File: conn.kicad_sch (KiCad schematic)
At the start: 73 parts, among them J10 MicroFit_2x04, J11 JST_S4B-XH, J12 MicroFit_2x04, J13 JST_B2B-XH, J14 JST_S2B-XH, J15 DNI, J16 MLX_1x03, J17 MLX_1x03, J5 JST_S6B-XH, J6 JST_S4B-XH, J7 MicroFit_2x04, J8 JST_S4B-XH, J9 JST_S4B-XH, SW2 DNI

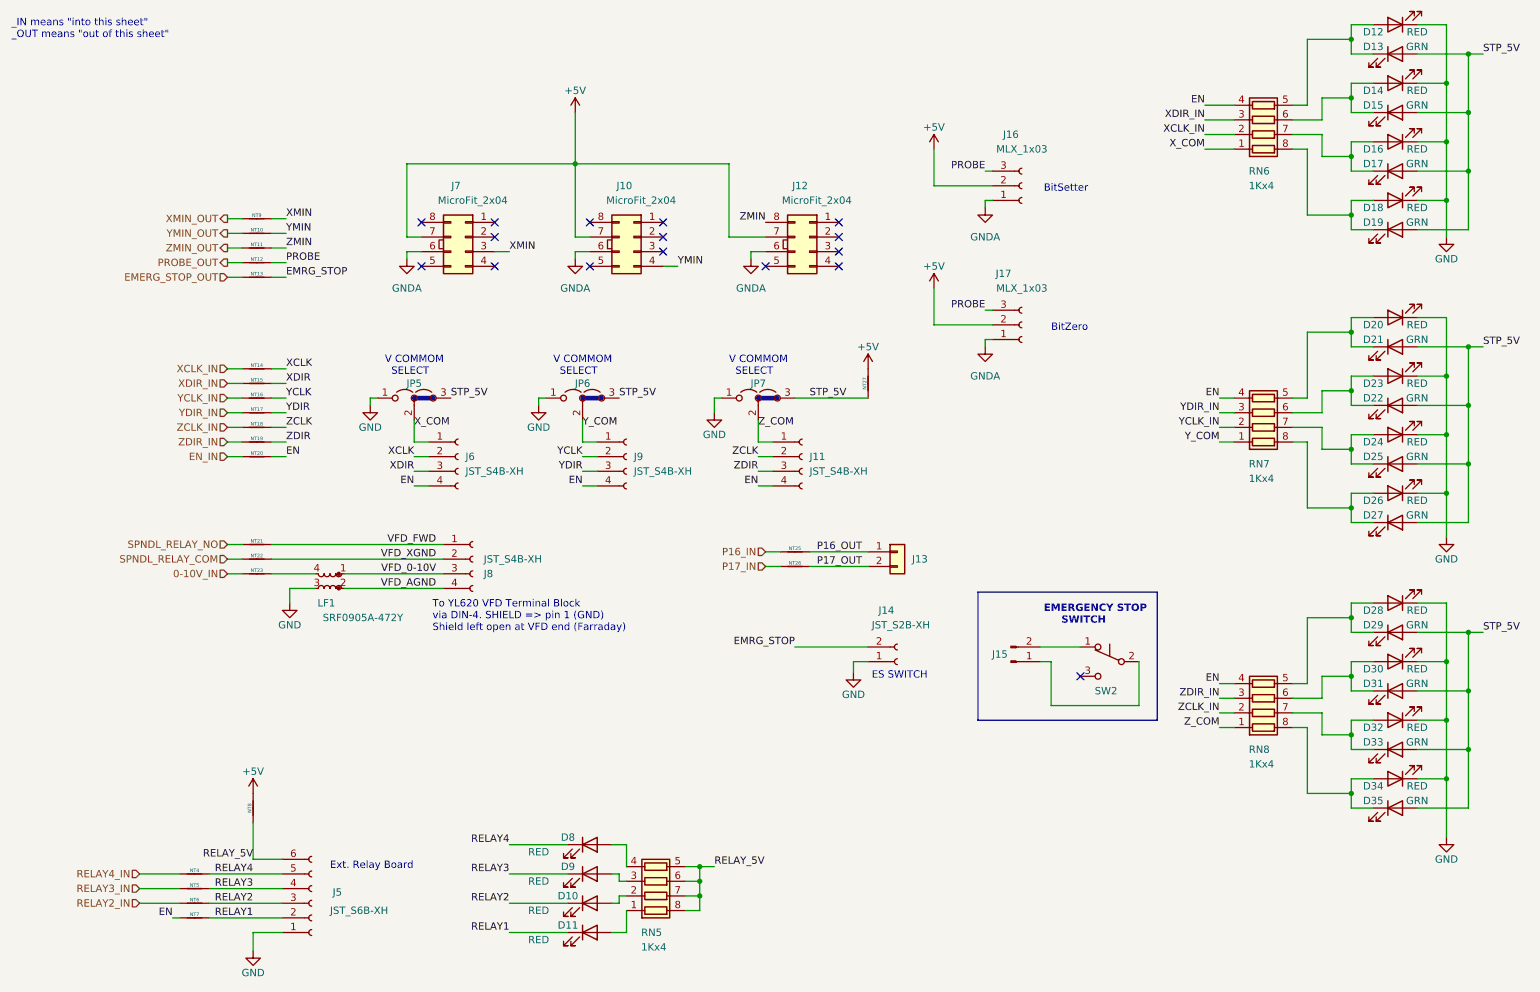
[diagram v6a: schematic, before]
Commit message: Completed change to screw terminal blocks. (P16/17 remains JST.)
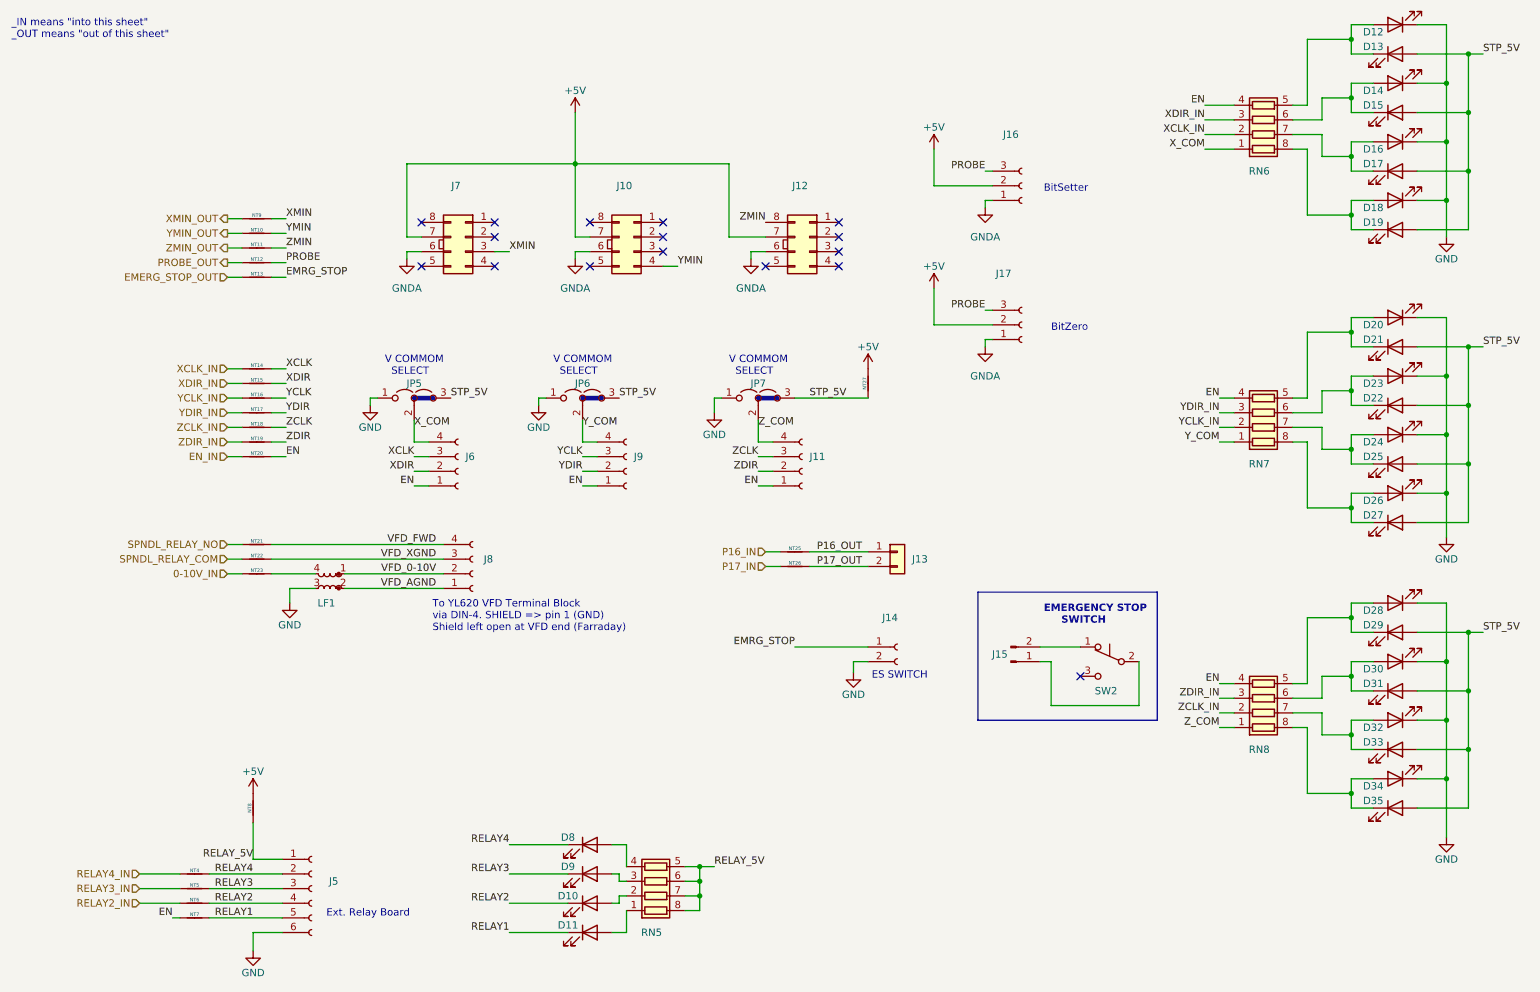
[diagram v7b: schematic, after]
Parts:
- D10, D11, D12, D14, D16, D18, D20, D22, D24, D26, D28, D30, D32, D34, D8, D9: value RED -> (none); footprint -Project:LED_0402_DOT -> (none)
- D13, D15, D17, D19, D21, D23, D25, D27, D29, D31, D33, D35: value GRN -> (none); footprint -Project:LED_0402_DOT -> (none)
- J10, J12, J7: value MicroFit_2x04 -> (none); footprint Connector_Molex:Molex_Micro-Fit_3.0_43045-0812_2x04_P3.00mm_Vertical -> (none)
- J11, J6, J8, J9: value JST_S4B-XH -> (none); footprint Connector_JST:JST_EH_S4B-EH_1x04_P2.50mm_Horizontal -> (none); E14MFR# S4B-EH(LF)(SN) -> (none); E14PART 1830721 -> (none); JLCMFR# S4B-XH-A(LF)(SN) -> (none); JLCPART C157925 -> (none)
- J13: value JST_B2B-XH -> (none); footprint Connector_JST:JST_EH_B2B-EH-A_1x02_P2.50mm_Vertical -> (none)
- J14: value JST_S2B-XH -> (none); footprint Connector_JST:JST_EH_S2B-EH_1x02_P2.50mm_Horizontal -> (none)
- J15, SW2: value DNI -> (none)
- J16, J17: value MLX_1x03 -> (none); footprint Connector_Molex:Molex_KK-254_AE-6410-03A_1x03_P2.54mm_Vertical -> (none)
- J5: value JST_S6B-XH -> (none); footprint Connector_JST:JST_EH_S6B-EH_1x06_P2.50mm_Horizontal -> (none); E14PART 1516282 -> (none); JLCMFR# S6B-XH-A(LF)(SN) -> (none); JLCPART C157919 -> (none)
- JP5, JP6, JP7: value Jumper_3_Open -> (none); footprint Connector_PinHeader_2.54mm:PinHeader_1x03_P2.54mm_Vertical -> (none)
- LF1: value SRF0905A-472Y -> (none); footprint Filter:Filter_Bourns_SRF0905_6.0x9.2mm -> (none)
- NT10, NT11, NT12, NT13, NT14, NT15, NT16, NT17, NT18, NT19, NT20, NT25, NT26, NT4, NT5, NT6, NT7, NT9: value DNI -> (none); footprint -Project:NetTie-2_SMD_Pad0.3mm -> (none)
- NT21, NT22, NT27, NT8: value DNI -> (none); footprint -Project:NetTie-2_SMD_Pad1.0mm -> (none)
- NT23: value DNI -> (none); footprint -Project:NetTie-2_SMD_Pad0.5mm -> (none)
- RN5, RN6, RN7, RN8: value 1Kx4 -> (none); footprint Resistor_SMD:R_Array_Convex_4x0603 -> (none)
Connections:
- net EMRG_STOP: now also J14.1 (Pin_1); no longer J14.2 (Pin_2)
- net EN: now also J11.1 (Pin_1), J6.1 (Pin_1), J9.1 (Pin_1); no longer J11.4 (Pin_4), J6.4 (Pin_4), J9.4 (Pin_4)
- net GND: now also J14.2 (Pin_2), J5.6 (Pin_6); no longer J14.1 (Pin_1), J5.1 (Pin_1)
- net RELAY1: now also J5.5 (Pin_5); no longer J5.2 (Pin_2)
- net RELAY2: now also J5.4 (Pin_4); no longer J5.3 (Pin_3)
- net RELAY3: now also J5.3 (Pin_3); no longer J5.4 (Pin_4)
- net RELAY4: now also J5.2 (Pin_2); no longer J5.5 (Pin_5)
- net RELAY_5V: now also J5.1 (Pin_1); no longer J5.6 (Pin_6)
- net VFD_0-10V: now also J8.2 (Pin_2); no longer J8.3 (Pin_3)
- net VFD_AGND: now also J8.1 (Pin_1); no longer J8.4 (Pin_4)
- net VFD_FWD: now also J8.4 (Pin_4); no longer J8.1 (Pin_1)
- net VFD_XGND: now also J8.3 (Pin_3); no longer J8.2 (Pin_2)
- net XCLK: now also J6.3 (Pin_3); no longer J6.2 (Pin_2)
- net XDIR: now also J6.2 (Pin_2); no longer J6.3 (Pin_3)
- net X_COM: now also J6.4 (Pin_4); no longer J6.1 (Pin_1)
- net YCLK: now also J9.3 (Pin_3); no longer J9.2 (Pin_2)
- net YDIR: now also J9.2 (Pin_2); no longer J9.3 (Pin_3)
- net Y_COM: now also J9.4 (Pin_4); no longer J9.1 (Pin_1)
- net ZCLK: now also J11.3 (Pin_3); no longer J11.2 (Pin_2)
- net ZDIR: now also J11.2 (Pin_2); no longer J11.3 (Pin_3)
- net Z_COM: now also J11.4 (Pin_4); no longer J11.1 (Pin_1)

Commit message: Changed name to Shapeoko LPT Interface v2.0
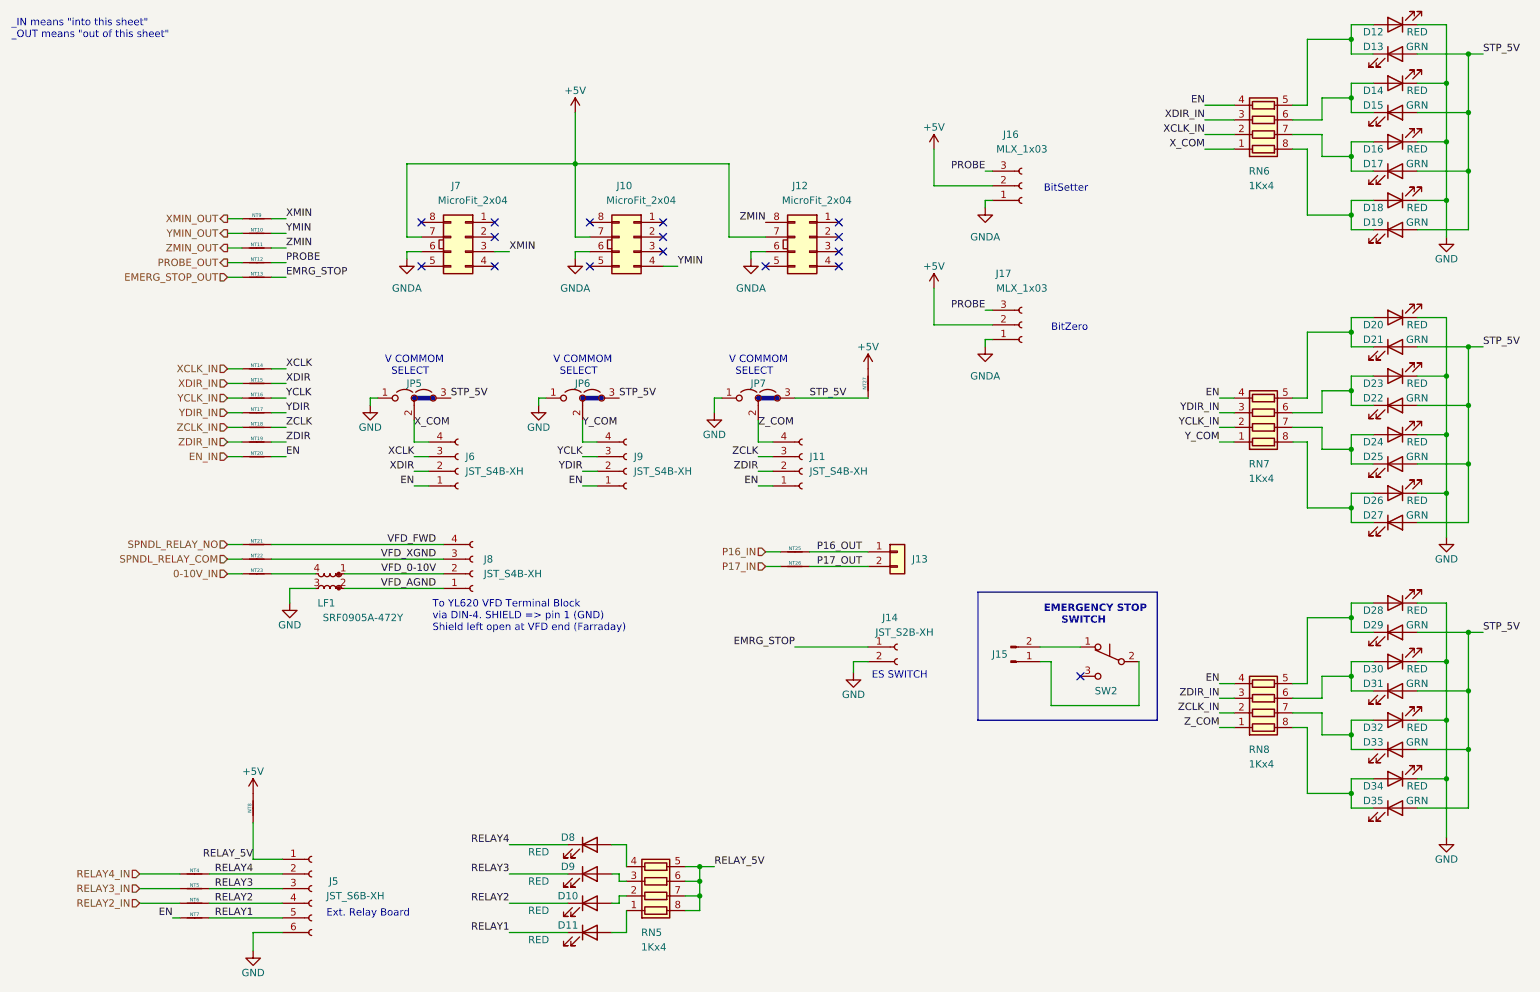
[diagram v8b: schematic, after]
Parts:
- D10, D11, D12, D14, D16, D18, D20, D22, D24, D26, D28, D30, D32, D34, D8, D9: value (none) -> RED; footprint (none) -> -Project:LED_0402_DOT
- D13, D15, D17, D19, D21, D23, D25, D27, D29, D31, D33, D35: value (none) -> GRN; footprint (none) -> -Project:LED_0402_DOT
- J10, J12, J7: value (none) -> MicroFit_2x04; footprint (none) -> Connector_Molex:Molex_Micro-Fit_3.0_43045-0812_2x04_P3.00mm_Vertical
- J11, J6, J8, J9: value (none) -> JST_S4B-XH; footprint (none) -> TerminalBlock_Phoenix:TerminalBlock_Phoenix_MPT-0,5-4-2.54_1x04_P2.54mm_Horizontal
- J13: value (none) -> JST_B2B-XH; footprint (none) -> Connector_JST:JST_EH_B2B-EH-A_1x02_P2.50mm_Vertical
- J14: value (none) -> JST_S2B-XH; footprint (none) -> TerminalBlock_Phoenix:TerminalBlock_Phoenix_MPT-0,5-2-2.54_1x02_P2.54mm_Horizontal
- J15, SW2: value (none) -> DNI
- J16, J17: value (none) -> MLX_1x03; footprint (none) -> Connector_Molex:Molex_KK-254_AE-6410-03A_1x03_P2.54mm_Vertical
- J5: value (none) -> JST_S6B-XH; footprint (none) -> TerminalBlock_Phoenix:TerminalBlock_Phoenix_MPT-0,5-6-2.54_1x06_P2.54mm_Horizontal
- JP5, JP6, JP7: value (none) -> Jumper_3_Open; footprint (none) -> Connector_PinHeader_2.54mm:PinHeader_1x03_P2.54mm_Vertical
- LF1: value (none) -> SRF0905A-472Y; footprint (none) -> Filter:Filter_Bourns_SRF0905_6.0x9.2mm
- NT10, NT11, NT12, NT13, NT14, NT15, NT16, NT17, NT18, NT19, NT20, NT25, NT26, NT4, NT5, NT6, NT7, NT9: value (none) -> DNI; footprint (none) -> -Project:NetTie-2_SMD_Pad0.3mm
- NT21: value (none) -> DNI; footprint (none) -> -Project:NetTie-2_SMD_Pad1.5mm
- NT22, NT27, NT8: value (none) -> DNI; footprint (none) -> -Project:NetTie-2_SMD_Pad1.0mm
- NT23: value (none) -> DNI; footprint (none) -> -Project:NetTie-2_SMD_Pad0.5mm
- RN5, RN6, RN7, RN8: value (none) -> 1Kx4; footprint (none) -> Resistor_SMD:R_Array_Convex_4x0603
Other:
- title: (none) -> Shapeoko LPT Interface — Connector
